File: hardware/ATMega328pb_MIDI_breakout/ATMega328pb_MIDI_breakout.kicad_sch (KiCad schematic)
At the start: 38 parts, among them J1 USB_B, J2 MIDI OUT, J3 MIDI IN, J4 I2C, J5 Conn_01x15_Male, J6 Conn_01x15_Male, J7 Barrel_Jack_Switch, Q1 2N3906, SW1 RotaryEncoder_Switch, SW2 SW_Push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

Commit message: MIDI Breakout Variations
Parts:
- removed Q1: 2N3906, Package_TO_SOT_THT:TO-92_Inline, symbol Device:Q_PNP_EBC
- added Q1: 2N3904, Package_TO_SOT_THT:TO-92_Inline, symbol Transistor_BJT:2N3904
- added R15: 1k, Resistor_THT:R_Axial_DIN0207_L6.3mm_D2.5mm_P7.62mm_Horizontal, symbol Device:R_Small_US
- R2: value 6k8 -> 1k
- R3: value 2k7 -> 1k
- R6: value 680 -> 220
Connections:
- net +5V: now also Q1.3 (C); no longer R3.1
- net GND: now also R3.2, R15.2
- net at R5.1: now also J3.5; no longer J3.4
- net at R1.1: now also J2.4; no longer J2.5
- net at D1.2 (A), U2.3 (C2): now also J3.4; no longer J3.5
- net at R4.2: now also J2.5; no longer J2.4
- net at R2.2: now also Q1.2 (B); no longer R3.2
- net at R4.1: now also R3.1, Q1.1 (E)
- net at U2.7 (VO1): now also R15.1
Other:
- moved on the sheet: R3

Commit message: Fixed MIDI pinout swap
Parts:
- added D2, D3: LED, LED_THT:LED_D5.0mm, symbol Device:LED
- added J8: I2C, Connector_PinHeader_2.54mm:PinHeader_1x04_P2.54mm_Vertical, symbol Connector:Conn_01x04_Male
- added J9: Conn_01x15_Male, Connector_PinHeader_2.54mm:PinHeader_1x15_P2.54mm_Vertical, symbol Connector:Conn_01x15_Male
- added R16, R17: 1k, Resistor_THT:R_Axial_DIN0207_L6.3mm_D2.5mm_P7.62mm_Horizontal, symbol Device:R_Small_US
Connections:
- net +5V: now also J8.2 (Pin_2), J9.3 (Pin_3)
- net +VDC: now also J9.1 (Pin_1)
- net GND: now also D2.1 (K), D3.1 (K), J8.1 (Pin_1), J9.2 (Pin_2)
- net SCL1: now also J8.4 (Pin_4), J9.13 (Pin_13)
- net SDA1: now also J8.3 (Pin_3), J9.14 (Pin_14)
- net at R5.1: now also J3.4; no longer J3.5
- net at D1.2 (A), U2.3 (C2): now also J3.5; no longer J3.4
- net at J6.10 (Pin_10), U1.21 (A2): now also J9.10 (Pin_10)
- net at J6.11 (Pin_11), U1.20 (A1): now also J9.11 (Pin_11)
- net at J6.12 (Pin_12), U1.19 (A0): now also J9.12 (Pin_12)
- net at J6.15 (Pin_15), U1.16 (D13): now also J9.15 (Pin_15)
- net at J6.4 (Pin_4), U1.27 (AREF): now also J9.4 (Pin_4)
- net at J6.5 (Pin_5), U1.26 (A7): now also J9.5 (Pin_5)
- net at J6.6 (Pin_6), U1.25 (A6): now also J9.6 (Pin_6)
- net at J6.7 (Pin_7), U1.24 (A5): now also J9.7 (Pin_7)
- net at J6.8 (Pin_8), U1.23 (A4): now also J9.8 (Pin_8)
- net at J6.9 (Pin_9), U1.22 (A3): now also J9.9 (Pin_9)
- net D7: now reaches J5.10 (Pin_10), U1.10 (D7)
- net D7: now also R17.1
- net D8: now reaches J5.11 (Pin_11), U1.11 (D8)
- net D8: now also R16.1
- new net: D2.2 (A), R16.2
- new net: D3.2 (A), R17.2

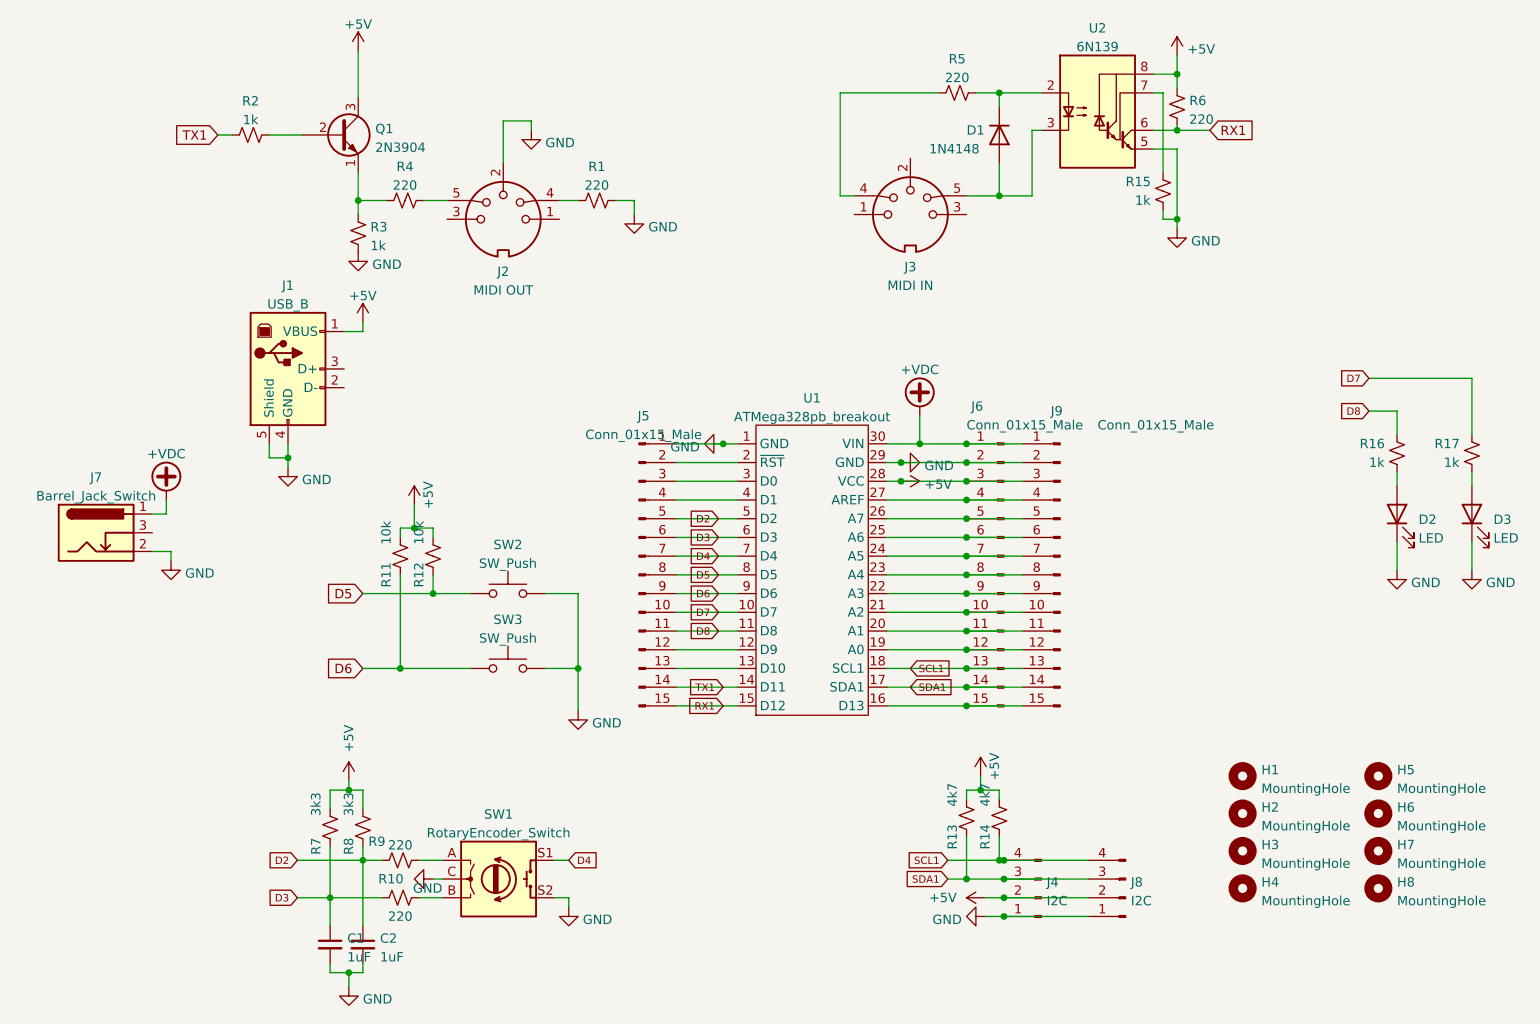
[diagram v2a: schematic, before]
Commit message: Fixes to Nano Breakout
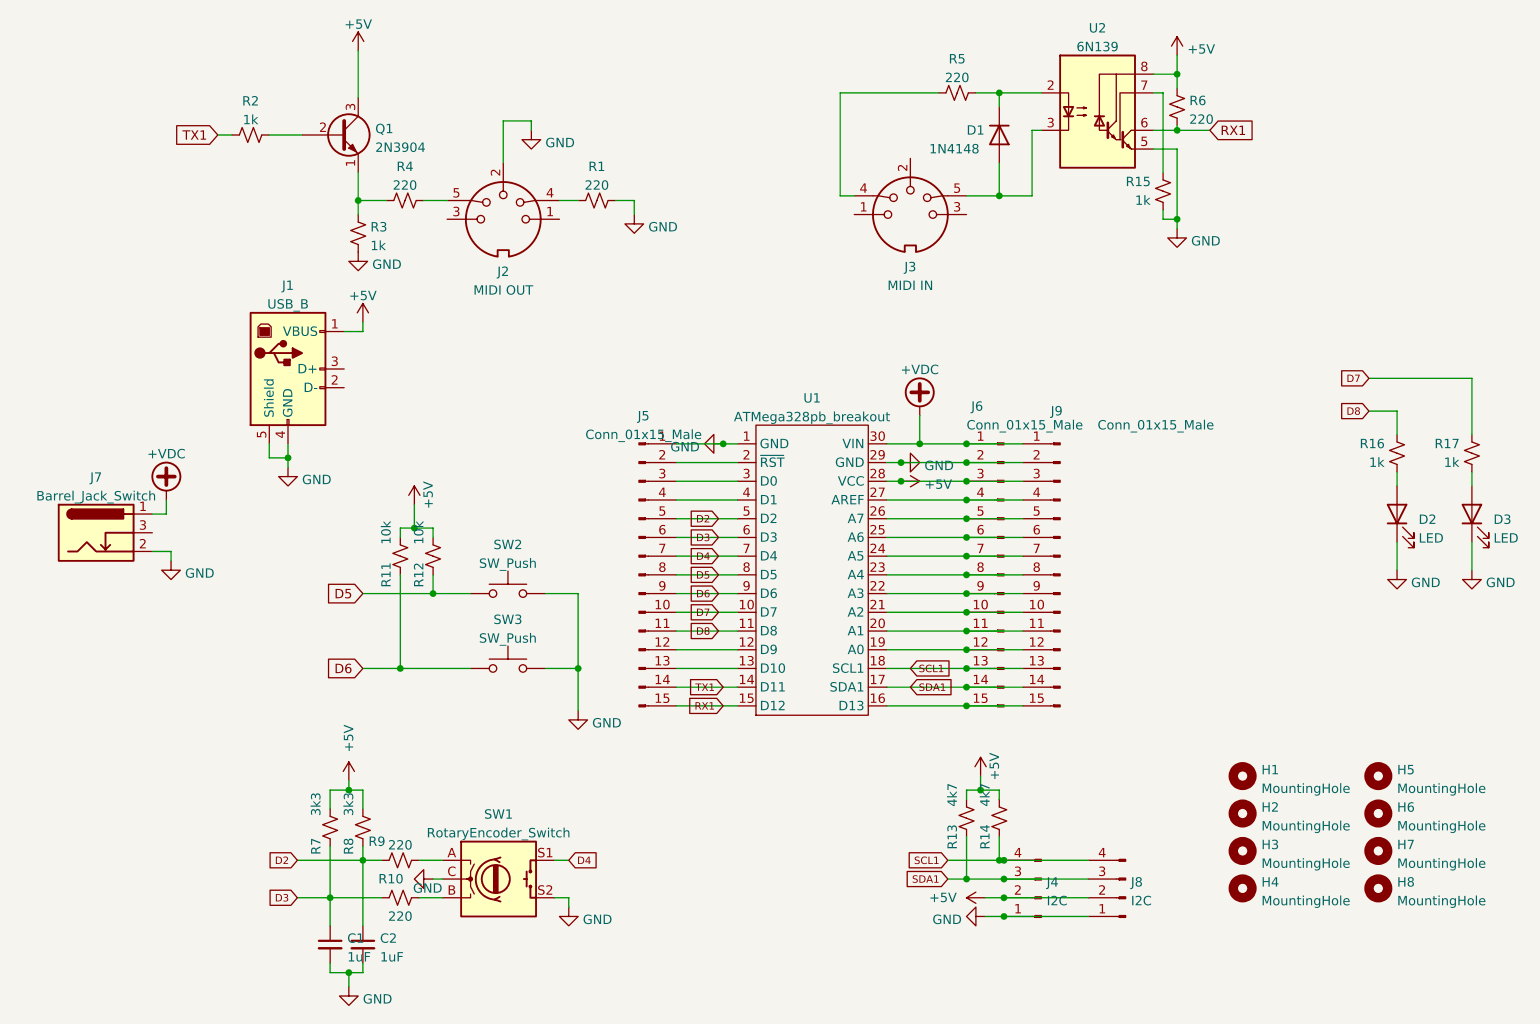
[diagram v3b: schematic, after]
